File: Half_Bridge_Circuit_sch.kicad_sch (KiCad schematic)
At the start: 25 parts, among them Q1 IRFZ44N, Q2 IRFZ44N, Q3 IRFZ44N, Q4 IRFZ44N, Q5 IRFZ44N, Q6 IRFZ44N, U1 IR2104, U2 IR2104, U3 IR2104

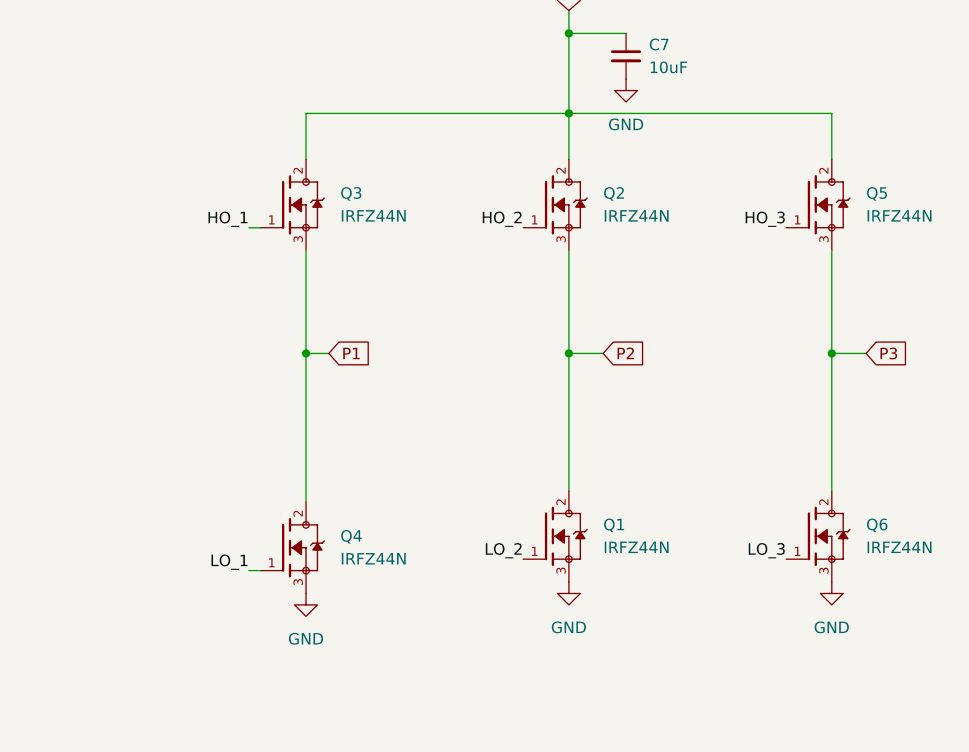
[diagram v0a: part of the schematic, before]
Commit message: Made progress on the PCB, and adressed small issues regarding the schematic
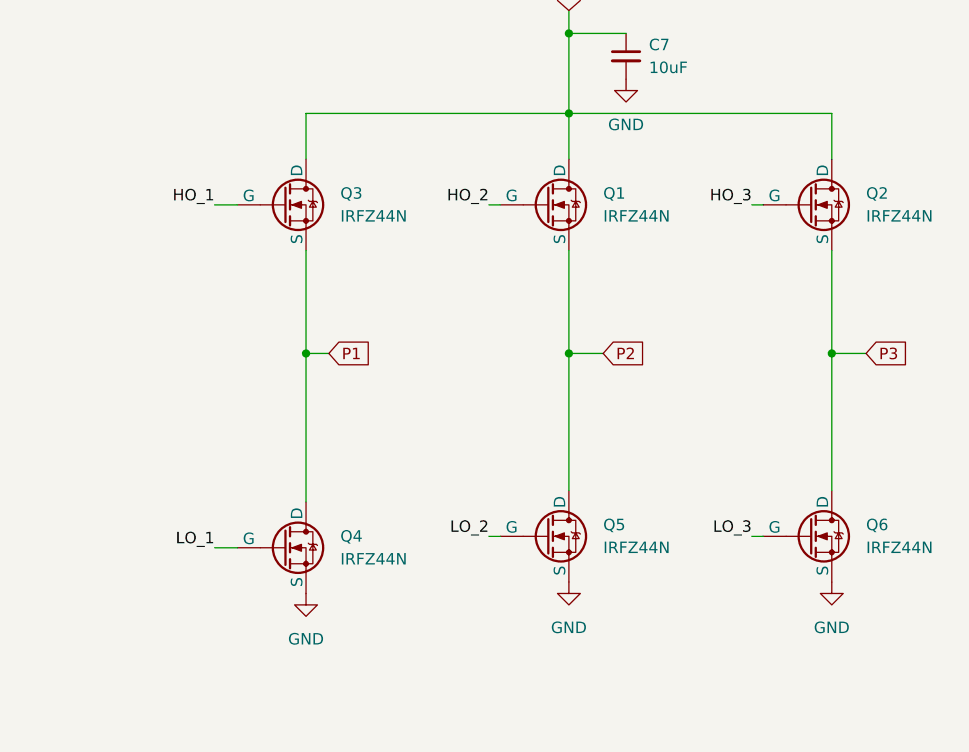
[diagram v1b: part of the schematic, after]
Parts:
- removed Q1, Q2, Q3, Q4, Q5, Q6: IRFZ44N, IRFZ44N:TO254P1016X419X2286-3, symbol IRFZ44N:IRFZ44N
- added Q1, Q2, Q3, Q4, Q5, Q6: IRFZ44N, Package_TO_SOT_THT:TO-220-3_Vertical, symbol Simulation_SPICE:NMOS
- C1, C4, C6: footprint (none) -> Ceramic_Cap_5.08mm_Spacing:Ceramic_Cap_5.08mm_Spacing
- C2, C3, C5, C7: footprint (none) -> Capacitor_THT:CP_Radial_D10.0mm_P5.00mm
- D1, D2, D3: footprint (none) -> Diode_THT:D_DO-35_SOD27_P7.62mm_Horizontal
- R10, R11, R12, R7, R8, R9: footprint (none) -> Resistor_THT:R_Axial_DIN0207_L6.3mm_D2.5mm_P10.16mm_Horizontal
- U1, U2, U3: footprint (none) -> Package_DIP:DIP-8_W7.62mm_Socket
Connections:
- net +VCC: now also Q1.2 (D), Q2.2 (D), Q3.2 (D)
- net GND: now also Q4.3 (S), Q5.3 (S), Q6.3 (S)
- net HO_1: now also Q3.1 (G)
- net HO_2: now also Q1.1 (G)
- net HO_3: now also Q2.1 (G)
- net LO_1: now also Q4.1 (G)
- net LO_2: now also Q5.1 (G)
- net LO_3: now also Q6.1 (G)
- net P1: now also Q3.3 (S), Q4.2 (D)
- net P2: now also Q1.3 (S), Q5.2 (D)
- net P3: now also Q2.3 (S), Q6.2 (D)

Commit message: Major design improvements to prototyping PCB
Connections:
- net P1: now also C1.2, U1.6 (VS)
- net P2: now also C4.2, U2.6 (VS)
- net P3: now also C6.2, U3.6 (VS)
- removed net VS: C1.2, C4.2, C6.2, U1.6 (VS), U2.6 (VS), U3.6 (VS)
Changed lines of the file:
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@@
+	(wire
+		(pts
+			(xy 218.44 95.25) (xy 220.98 95.25)
+		)
+		(stroke
+			(width 0)
+			(type default)
+		)
+	)
 	(wire
 		(pts
@@
 	(wire
 		(pts
+			(xy 189.23 95.25) (xy 191.77 95.25)
+		)
+		(stroke
+			(width 0)
+			(type default)
+		)
+	)
+	(wire
+		(pts
 			(xy 162.56 68.58) (xy 162.56 73.66)
 		)
@@
 		(pts
 			(xy 114.3 162.56) (xy 114.3 168.91)
+		)
+		(stroke
+			(width 0)
+			(type default)
+		)
+	)
+	(wire
+		(pts
+			(xy 158.75 95.25) (xy 162.56 95.25)
 		)
 		(stroke
@@
 		)
 	)
-	(label "VS"
+	(label "VS1"
 		(at 116.84 54.61 0)
 		(fields_autoplaced yes)
@@
 		)
 	)
-	(label "VS"
+	(label "VS2"
+		(at 189.23 95.25 180)
+		(fields_autoplaced yes)
+		(effects
+			(font
+				(size 1.27 1.27)
+			)
+			(justify right bottom)
+		)
+	)
+	(label "VS3"
 		(at 119.38 168.91 0)
 		(fields_autoplaced yes)
@@
 		)
 	)
+	(label "VS1"
+		(at 158.75 95.25 180)
+		(fields_autoplaced yes)
+		(effects
+			(font
+				(size 1.27 1.27)
+			)
+			(justify right bottom)
+		)
+	)
+	(label "VS3"
+		(at 218.44 95.25 180)
+		(fields_autoplaced yes)
+		(effects
+			(font
+				(size 1.27 1.27)
+			)
+			(justify right bottom)
+		)
+	)
 	(label "HO_1"
 		(at 152.4 78.74 180)
@@
 		)
 	)
-	(label "VS"
+	(label "VS2"
 		(at 118.11 110.49 0)
 		(fields_autoplaced yes)

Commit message: Fixed minor inconsistencies, improved orginization, MOSFET gate resistors calculted.
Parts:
- R10, R11, R12, R7, R8, R9: value R_US -> 47Ω
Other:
- note removed: "Gate Resistors to be calculated"
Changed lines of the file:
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@@
 		(title "Motor Driver - Half Bridge Circuit")
 		(date "2024-09-07")
-		(rev "1")
+		(rev "2")
 		(company "Andrew Fischer")
 	)
@@
 		)
 	)
-	(text "Gate Resistors to be calculated\n"
-		(exclude_from_sim no)
-		(at 112.34 62.7367 0)
-		(effects
-			(font
-				(size 1.27 1.27)
-			)
-		)
-	)
 	(label "VS1"
 		(at 116.84 54.61 0)
@@
 			)
 		)
-		(property "Value" "R_US"
+		(property "Value" "47Ω"
 			(at 102.87 154.94 90)
 			(effects
@@
 			)
 		)
-		(property "Value" "R_US"
+		(property "Value" "47Ω"
 			(at 102.87 96.52 90)
 			(effects
@@
 			)
 		)
-		(property "Value" "R_US"
+		(property "Value" "47Ω"
 			(at 102.87 53.34 90)
 			(effects
@@
 			)
 		)
-		(property "Value" "R_US"
+		(property "Value" "47Ω"
 			(at 102.87 40.64 90)
 			(effects
@@
 			)
 		)
-		(property "Value" "R_US"
+		(property "Value" "47Ω"
 			(at 102.87 109.22 90)
 			(effects
@@
 			)
 		)
-		(property "Value" "R_US"
+		(property "Value" "47Ω"
 			(at 102.87 167.64 90)
 			(effects

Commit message: Removed alot of redundent VIAs, added testpoints, cleaned up some traces
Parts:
- added TP21, TP22, TP23, TP34, TP35, TP36: TestPoint, TestPoint:TestPoint_THTPad_1.0x1.0mm_Drill0.5mm, symbol Connector:TestPoint
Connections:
- net P1: now also TP34.1
- net P2: now also TP35.1
- net P3: now also TP36.1
- net at C4.1, D2.1 (K), U2.8 (VB): now also TP22.1
- net at C1.1, D1.1 (K), U1.8 (VB): now also TP21.1
- net at C6.1, D3.1 (K), U3.8 (VB): now also TP23.1

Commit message: Reviewed gate resistors and removed MOSFET driver resistor
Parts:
- R10, R11, R12, R7, R8, R9: value 47Ω -> 10Ω
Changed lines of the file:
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@@
 			)
 		)
-		(property "Value" "47Ω"
+		(property "Value" "10Ω"
 			(at 102.87 154.94 90)
 			(effects
@@
 			)
 		)
-		(property "Value" "47Ω"
+		(property "Value" "10Ω"
 			(at 102.87 96.52 90)
 			(effects
@@
 			)
 		)
-		(property "Value" "47Ω"
+		(property "Value" "10Ω"
 			(at 102.87 53.34 90)
 			(effects
@@
 			)
 		)
-		(property "Value" "47Ω"
+		(property "Value" "10Ω"
 			(at 102.87 40.64 90)
 			(effects
@@
 			)
 		)
-		(property "Value" "47Ω"
+		(property "Value" "10Ω"
 			(at 102.87 109.22 90)
 			(effects
@@
 			)
 		)
-		(property "Value" "47Ω"
+		(property "Value" "10Ω"
 			(at 102.87 167.64 90)
 			(effects

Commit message: Prototyping PCB Ordered!
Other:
- note added: "Same idea with the gate resistors here."
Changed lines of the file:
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@@
+		)
+	)
+	(text "Same idea with the gate resistors here.\n"
+		(exclude_from_sim no)
+		(at 140.716 43.688 0)
+		(effects
+			(font
+				(size 1.27 1.27)
+			)
 		)
 	)
